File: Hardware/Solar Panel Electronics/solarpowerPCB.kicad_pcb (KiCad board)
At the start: 4 copper layers, 141 parts, among them J1 Screw_Terminal_SolarPanel_Inp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, J10 Screw_Terminal_SolarPanel_Inp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, J11 Screw_Terminal_SolarPanel_Inp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, J12 NTC Connector, J13 Battery Connector, J14 Screw_Terminal_5VRail, J2 Screw_Terminal_SolarPanel_Inp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, J3 Conn_01x02_Male, J4 Conn_01x06_Male, J5 Conn_01x02_Male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

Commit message: PCB layout
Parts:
- moved J7 1.55 mm to (41.3, 132.8)
- turned U1 to 90 degrees
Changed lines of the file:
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@@
   )
   (footprint "Package_SO:SOIC-8_3.9x4.9mm_P1.27mm" (layer "F.Cu")
-    (at 55.626 114.808)
+    (at 55.626 114.808 90)
     (descr "SOIC, 8 Pin (JEDEC MS-012AA, https://www.analog.com/media/en/package-pcb-resources/package/pkg_pdf/soic_narrow-r/r_8.pdf), generated with kicad-footprint-generator ipc_gullwing_generator.py")
     (tags "SOIC SO")
@@
     (property "Sheetname" "")
     (attr smd)
-    (fp_text reference "U1" (at 0 -3.4) (layer "F.SilkS")
-      (effects (font (size 1 1) (thickness 0.15)))
-    )
-    (fp_text value "SN65HVD230" (at 0 2.892) (layer "F.Fab")
-      (effects (font (size 1 1) (thickness 0.15)))
-    )
-    (fp_text user "${REFERENCE}" (at 0 0) (layer "F.Fab")
+    (fp_text reference "U1" (at 0 -3.4 90) (layer "F.SilkS")
+      (effects (font (size 1 1) (thickness 0.15)))
+    )
+    (fp_text value "SN65HVD230" (at 0 2.892 90) (layer "F.Fab")
+      (effects (font (size 1 1) (thickness 0.15)))
+    )
+    (fp_text user "${REFERENCE}" (at 0 0 90) (layer "F.Fab")
       (effects (font (size 0.98 0.98) (thickness 0.15)))
     )
@@
     (fp_line (start -1.95 2.45) (end -1.95 -1.475) (layer "F.Fab") (width 0.1))
     (fp_line (start -0.975 -2.45) (end 1.95 -2.45) (layer "F.Fab") (width 0.1))
-    (pad "1" smd roundrect (at -2.475 -1.905) (size 1.95 0.6) (layers "F.Cu" "F.Paste" "F.Mask") (roundrect_rratio 0.25)
+    (pad "1" smd roundrect (at -2.475 -1.905 90) (size 1.95 0.6) (layers "F.Cu" "F.Paste" "F.Mask") (roundrect_rratio 0.25)
       (net 8 "Net-(C6-Pad2)") (pinfunction "D") (pintype "input"))
-    (pad "2" smd roundrect (at -2.475 -0.635) (size 1.95 0.6) (layers "F.Cu" "F.Paste" "F.Mask") (roundrect_rratio 0.25)
+    (pad "2" smd roundrect (at -2.475 -0.635 90) (size 1.95 0.6) (layers "F.Cu" "F.Paste" "F.Mask") (roundrect_rratio 0.25)
       (net 3 "GND") (pinfunction "GND") (pintype "power_in"))
-    (pad "3" smd roundrect (at -2.475 0.635) (size 1.95 0.6) (layers "F.Cu" "F.Paste" "F.Mask") (roundrect_rratio 0.25)
+    (pad "3" smd roundrect (at -2.475 0.635 90) (size 1.95 0.6) (layers "F.Cu" "F.Paste" "F.Mask") (roundrect_rratio 0.25)
       (net 2 "+3V3") (pinfunction "VCC") (pintype "power_in"))
-    (pad "4" smd roundrect (at -2.475 1.905) (size 1.95 0.6) (layers "F.Cu" "F.Paste" "F.Mask") (roundrect_rratio 0.25)
+    (pad "4" smd roundrect (at -2.475 1.905 90) (size 1.95 0.6) (layers "F.Cu" "F.Paste" "F.Mask") (roundrect_rratio 0.25)
       (net 75 "Net-(R2-Pad2)") (pinfunction "R") (pintype "output"))
-    (pad "5" smd roundrect (at 2.475 1.905) (size 1.95 0.6) (layers "F.Cu" "F.Paste" "F.Mask") (roundrect_rratio 0.25)
+    (pad "5" smd roundrect (at 2.475 1.905 90) (size 1.95 0.6) (layers "F.Cu" "F.Paste" "F.Mask") (roundrect_rratio 0.25)
       (net 61 "/Vref") (pinfunction "Vref") (pintype "output"))
-    (pad "6" smd roundrect (at 2.475 0.635) (size 1.95 0.6) (layers "F.Cu" "F.Paste" "F.Mask") (roundrect_rratio 0.25)
+    (pad "6" smd roundrect (at 2.475 0.635 90) (size 1.95 0.6) (layers "F.Cu" "F.Paste" "F.Mask") (roundrect_rratio 0.25)
       (net 14 "/CAN_LOW") (pinfunction "CANL") (pintype "bidirectional"))
-    (pad "7" smd roundrect (at 2.475 -0.635) (size 1.95 0.6) (layers "F.Cu" "F.Paste" "F.Mask") (roundrect_rratio 0.25)
+    (pad "7" smd roundrect (at 2.475 -0.635 90) (size 1.95 0.6) (layers "F.Cu" "F.Paste" "F.Mask") (roundrect_rratio 0.25)
       (net 13 "/CAN_HIGH") (pinfunction "CANH") (pintype "bidirectional"))
-    (pad "8" smd roundrect (at 2.475 -1.905) (size 1.95 0.6) (layers "F.Cu" "F.Paste" "F.Mask") (roundrect_rratio 0.25)
+    (pad "8" smd roundrect (at 2.475 -1.905 90) (size 1.95 0.6) (layers "F.Cu" "F.Paste" "F.Mask") (roundrect_rratio 0.25)
       (net 76 "Net-(R3-Pad1)") (pinfunction "Rs") (pintype "input"))
     (model "${KICAD6_3DMODEL_DIR}/Package_SO.3dshapes/SOIC-8_3.9x4.9mm_P1.27mm.wrl"
@@
   )
   (footprint "Connector_Card:microSD_HC_Wuerth_693072010801" (layer "F.Cu")
-    (at 42.8565 132.588 90)
+    (at 41.3325 132.842 90)
     (descr "http://katalog.we-online.de/em/datasheet/693072010801.pdf")
     (tags "Micro SD Wuerth Wurth Würth")

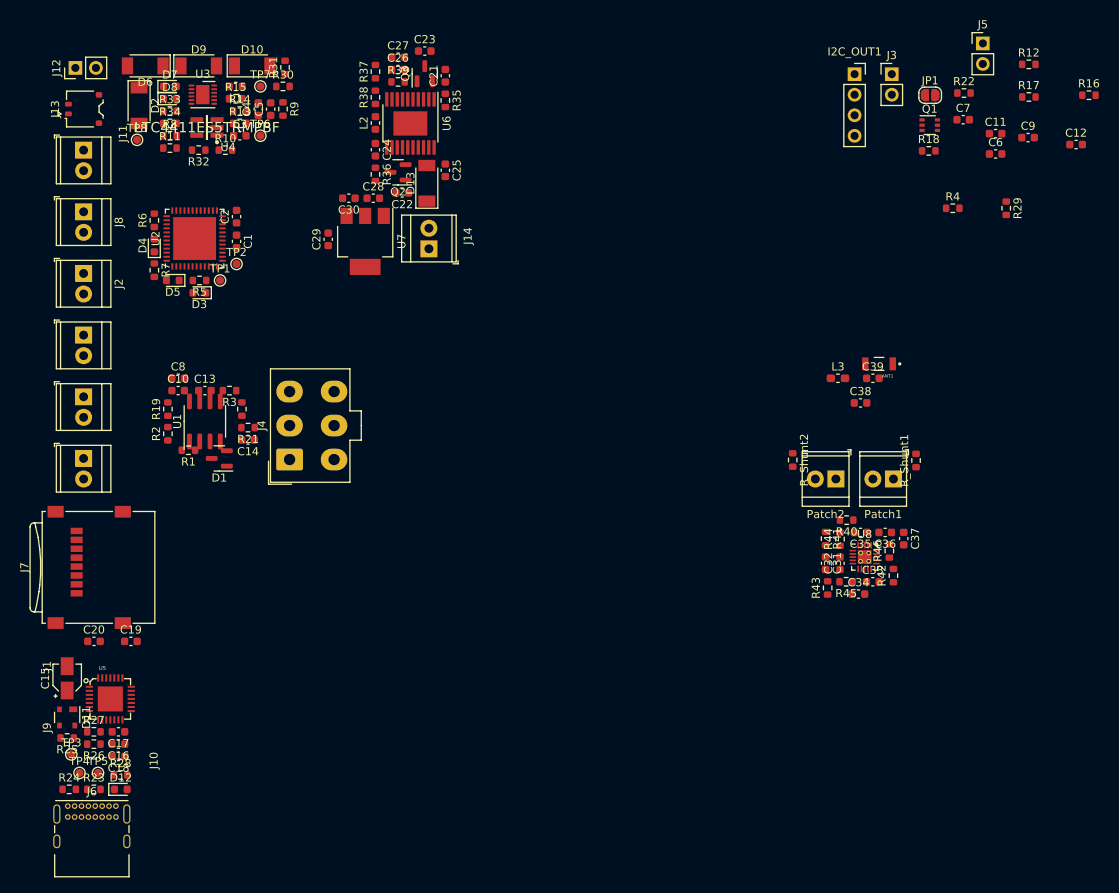
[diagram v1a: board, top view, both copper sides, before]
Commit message: Preliminary Layout done. (46x77mm)
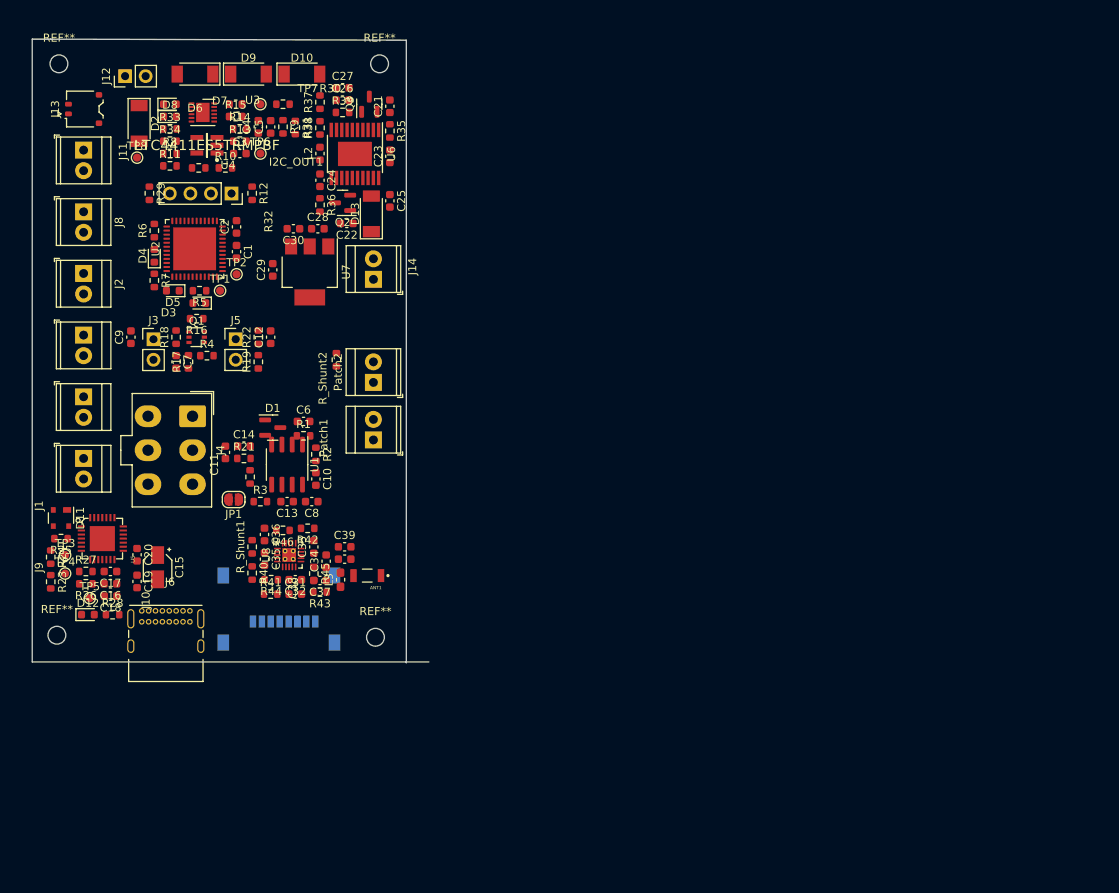
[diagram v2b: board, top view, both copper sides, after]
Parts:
- added REF**: MountingHole_2.2mm_M2, MountingHole:MountingHole_2.2mm_M2, F.Cu at (37.6, 70.6)
- added REF**: MountingHole_2.2mm_M2, MountingHole:MountingHole_2.2mm_M2, F.Cu at (76.7, 141.5)
- added REF**: MountingHole_2.2mm_M2, MountingHole:MountingHole_2.2mm_M2, F.Cu at (77.2, 70.6)
- added REF**: MountingHole_2.2mm_M2, MountingHole:MountingHole_2.2mm_M2, F.Cu at (37.3, 141.2)
- J7: moved to B.Cu
- moved R16 113.7 mm to (54.6, 102.1), turned to 180 degrees
- moved C9 113.6 mm to (46.5, 104.4), turned to 90 degrees
- moved R17 108.9 mm to (53.6, 107.4), turned to 90 degrees
- moved R29 105.9 mm to (48.8, 86.6)
- moved C11 103.0 mm to (58.2, 118.6), turned to 90 degrees
- moved C12 102.3 mm to (63.8, 104.4), turned to 90 degrees
- moved C7 101.8 mm to (52.1, 107.4), turned to -90 degrees
- moved JP1 99.5 mm to (59.2, 124.5), turned to 180 degrees
- moved J5 99.3 mm to (59.4, 104.6)
- moved R12 97.3 mm to (61.5, 86.6), turned to -90 degrees
- moved J3 96.9 mm to (49.3, 104.6)
- moved R18 95.8 mm to (52.1, 104.4), turned to 90 degrees
- moved Q1 94.3 mm to (54.6, 104.4)
- moved R4 94.0 mm to (55.9, 106.7)
- moved R22 92.3 mm to (62.2, 104.4), turned to 90 degrees
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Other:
- board outline added: 49 x 77.1 mm

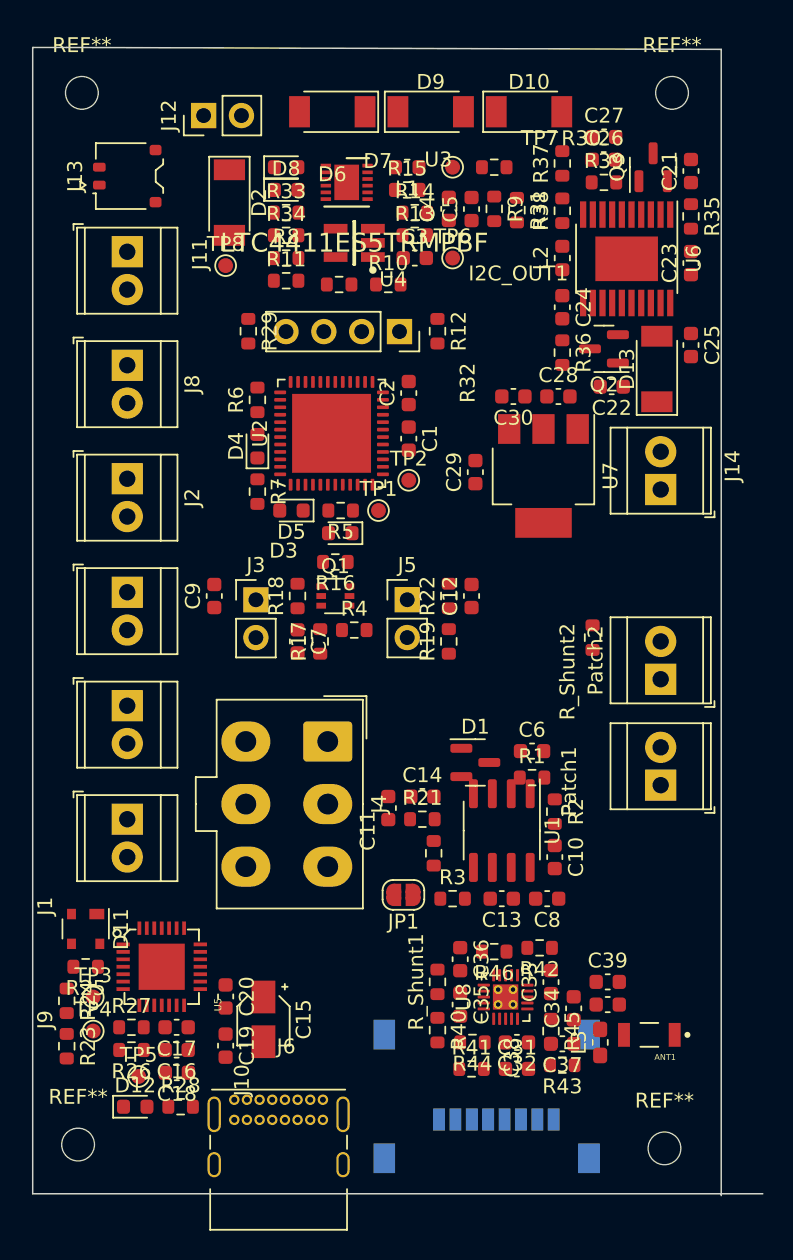
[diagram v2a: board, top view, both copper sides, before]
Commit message: Fix edge cuts
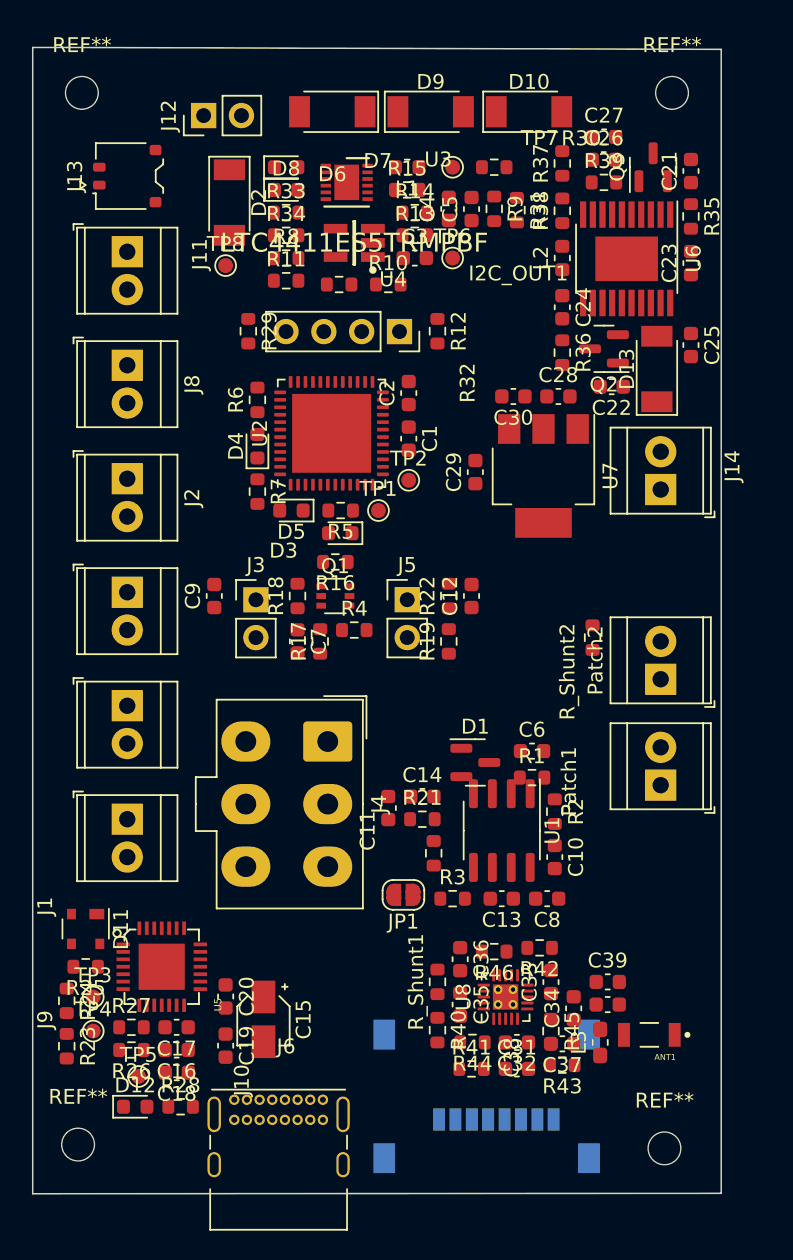
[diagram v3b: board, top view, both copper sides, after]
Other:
- board size 49 x 77.1 mm -> 46.2 x 77 mm
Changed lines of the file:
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@@
       (effects (font (size 1 1) (thickness 0.15)))
     )
-    (fp_text value "MountingHole_2.2mm_M2" (at 0 3.2) (layer "F.Fab")
+    (fp_text value "MountingHole_2.2mm_M2" (at 0.042 5.022) (layer "F.Fab")
       (effects (font (size 1 1) (thickness 0.15)))
     )
@@
     )
   )
-  (gr_line (start 83.312 144.526) (end 34.29 144.526) (layer "Edge.Cuts") (width 0.1))
-  (gr_line (start 80.518 67.691) (end 80.518 144.653) (layer "Edge.Cuts") (width 0.1))
+  (gr_line (start 80.518 144.5) (end 34.29 144.526) (layer "Edge.Cuts") (width 0.1))
+  (gr_line (start 80.518 67.691) (end 80.518 144.5) (layer "Edge.Cuts") (width 0.1))
   (gr_line (start 34.29 144.526) (end 34.29 67.564) (layer "Edge.Cuts") (width 0.1))
   (gr_line (start 34.29 67.564) (end 36.576 67.564) (layer "Edge.Cuts") (width 0.1))
